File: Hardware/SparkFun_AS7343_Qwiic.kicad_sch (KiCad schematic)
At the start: 38 parts, among them J1 Qwiic_RA, J2 Qwiic_RA, J3 Conn_01x06, Q1 BSS138, Q2 BSS138, U1 RT9080-1.8V, U2 AS7343

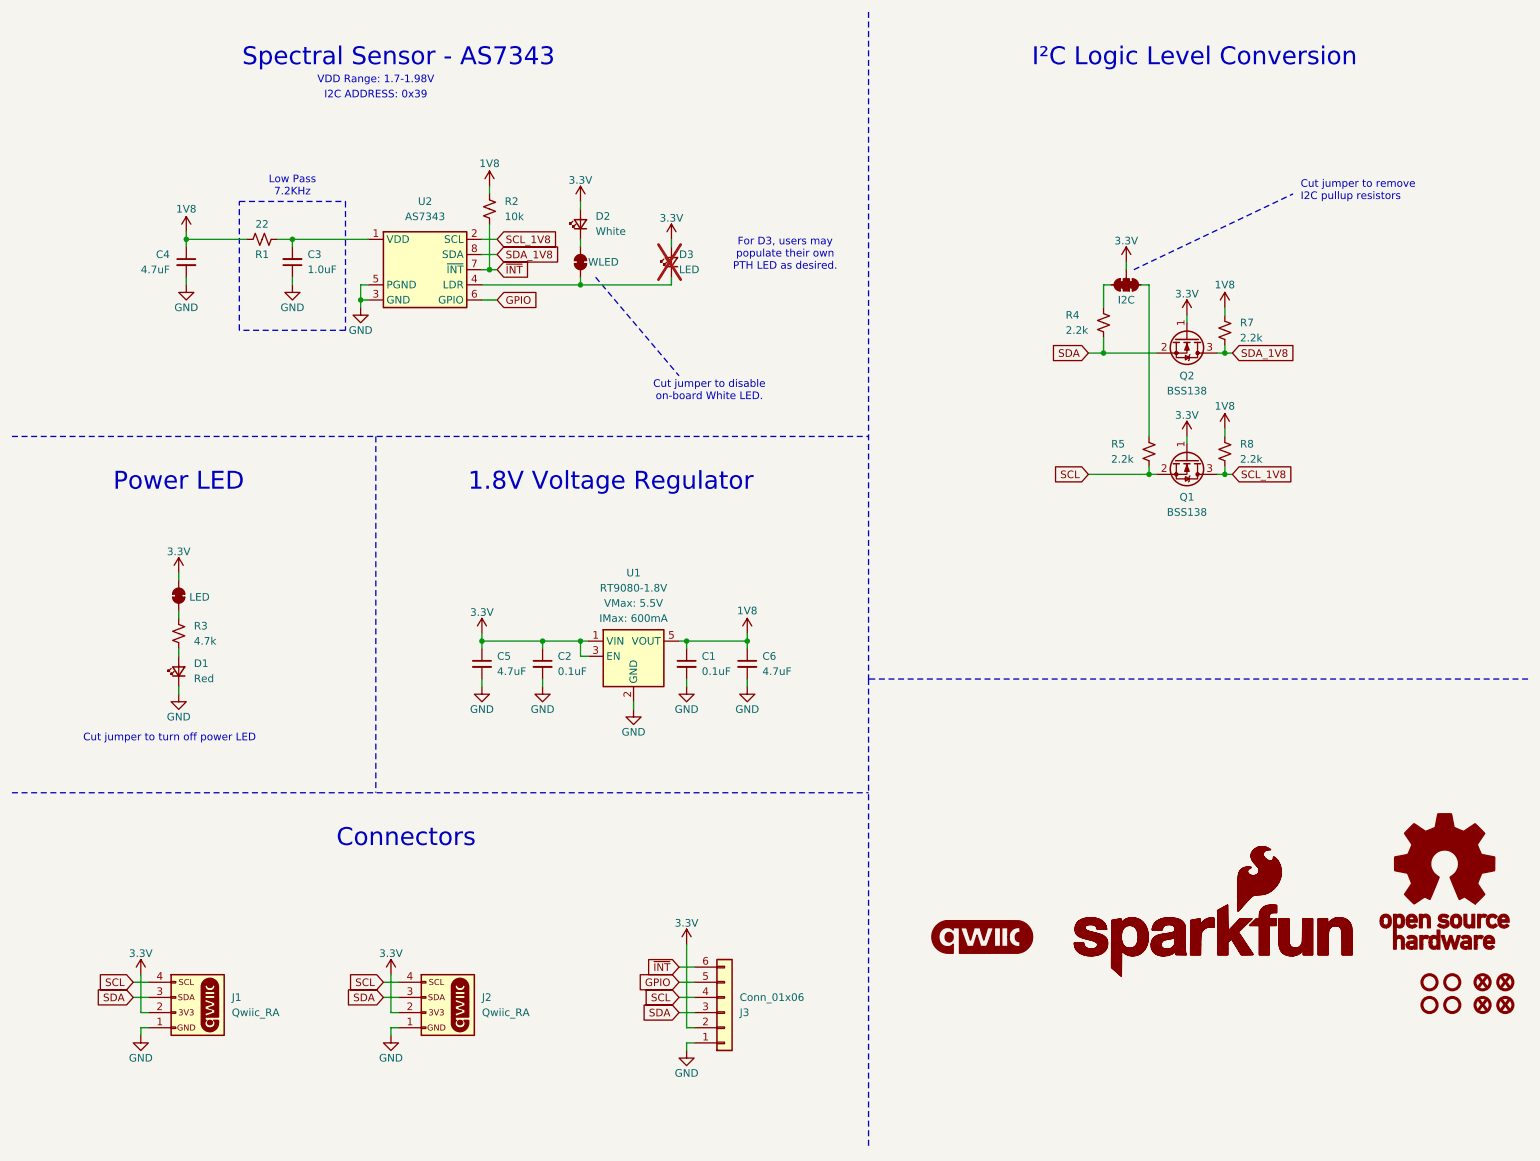
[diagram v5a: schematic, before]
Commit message: more review notes
-changed 1V8 to 1.8V to match style of 3.3V
-corrected schematic note for low pass filter. Is kHz, was KHz
-removed one of the QWIIC logos
-Moved OSHW to bottom silk
-aligned PWR LED silk label exactly with Y val of LED.
-changed sch note about i2c address to be "7-bit unshifted I2C address: 0x39"
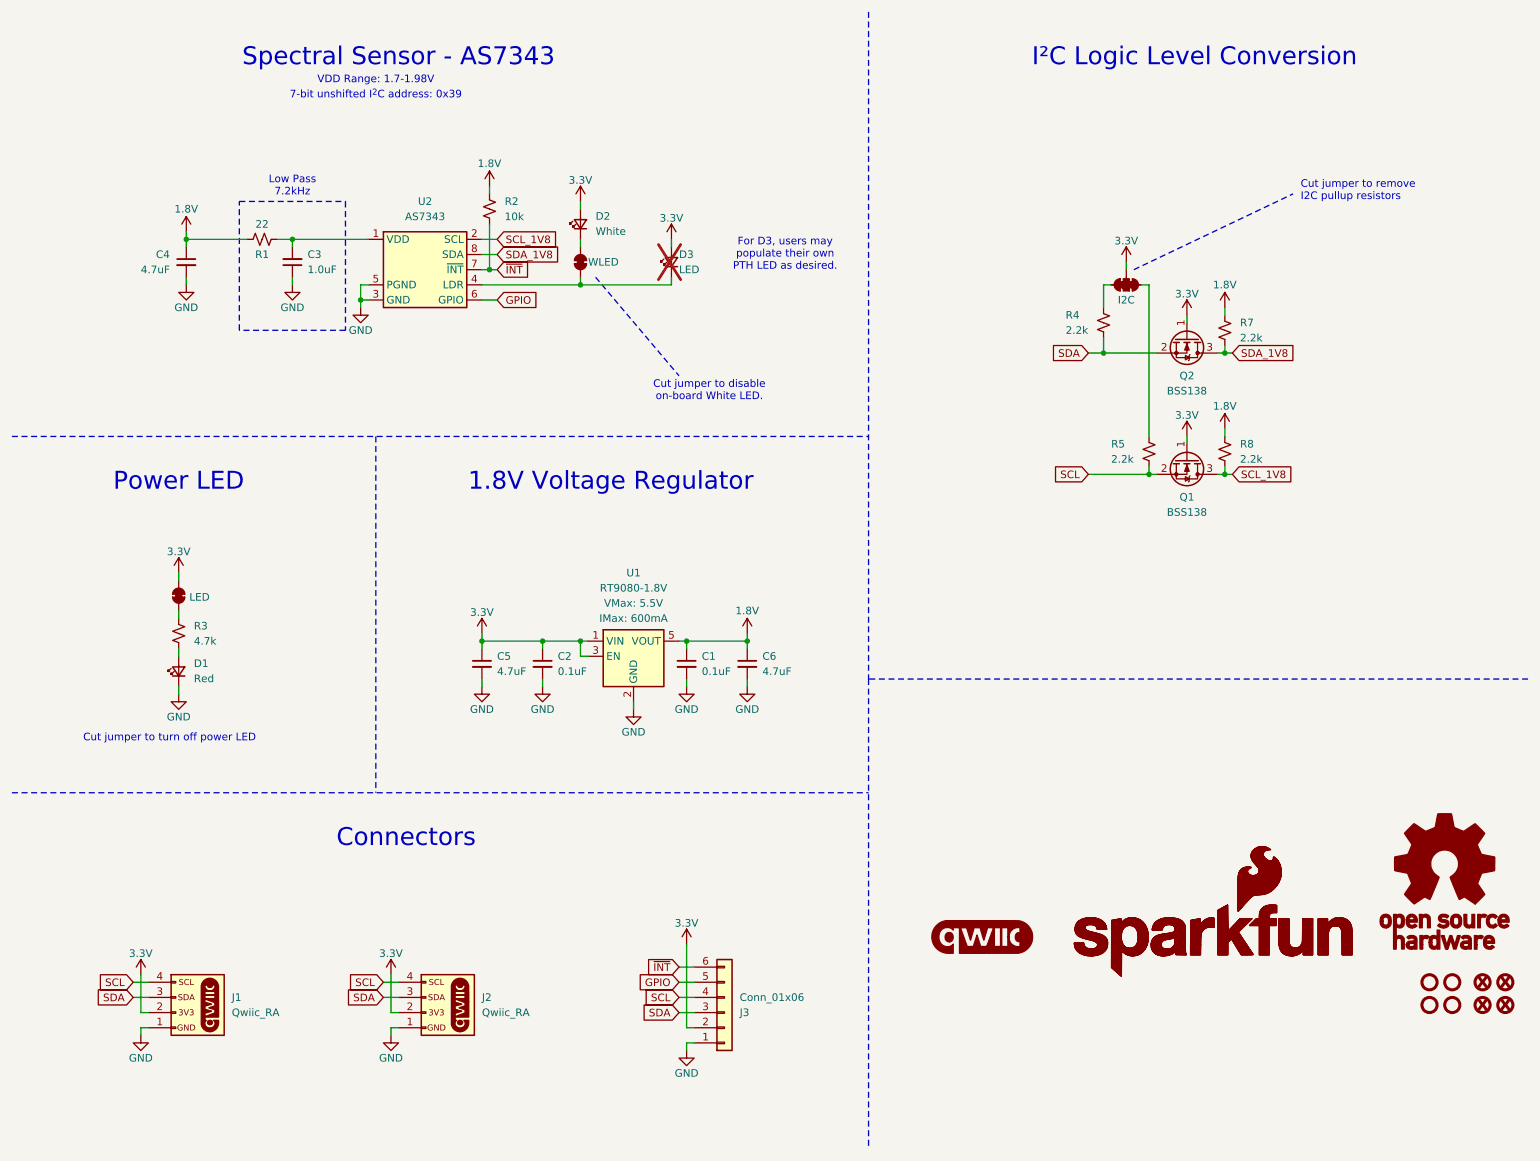
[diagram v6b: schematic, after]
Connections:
- net 1V8 renamed 1.8V
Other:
- note added: "7-bit unshifted I^{2}C address: 0x39"
- note added: "Low Pass 7.2kHz"
- note removed: "I2C ADDRESS: 0x39"
- note removed: "Low Pass 7.2KHz"
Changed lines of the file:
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@@
 		(comment 2 "Designed by: P. Lewis")
 	)
-	(text "Low Pass\n7.2KHz"
+	(text "Low Pass\n7.2kHz"
 		(exclude_from_sim no)
 		(at 59.69 41.91 0)
@@
 		)
 	)
-	(text "I2C ADDRESS: 0x39"
+	(text "7-bit unshifted I^{2}C address: 0x39"
 		(exclude_from_sim no)
 		(at 73.66 26.67 0)
@@
 			)
 		)
-		(property "Value" "1V8"
+		(property "Value" "1.8V"
 			(at 135.89 113.03 0)
 			(do_not_autoplace yes)
@@
 			)
 		)
-		(property "Value" "1V8"
+		(property "Value" "1.8V"
 			(at 215.9 78.74 0)
 			(do_not_autoplace yes)
@@
 			)
 		)
-		(property "Value" "1V8"
+		(property "Value" "1.8V"
 			(at 215.9 58.42 0)
 			(do_not_autoplace yes)
@@
 			)
 		)
-		(property "Value" "1V8"
+		(property "Value" "1.8V"
 			(at 41.91 45.72 0)
 			(do_not_autoplace yes)
@@
 			)
 		)
-		(property "Value" "1V8"
+		(property "Value" "1.8V"
 			(at 92.71 38.1 0)
 			(do_not_autoplace yes)

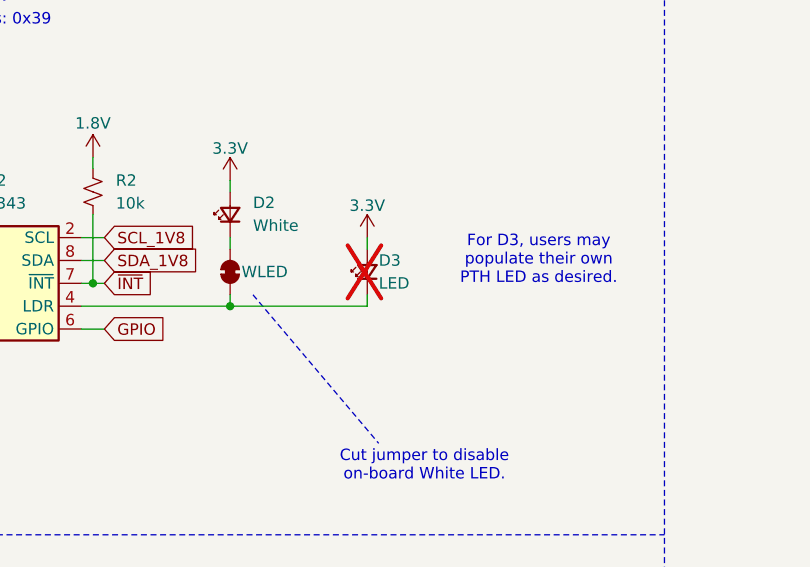
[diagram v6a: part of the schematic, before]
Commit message: added USER LED label to bottom silk
-changed value ot D3 to "USER"
-added silk label to bottom for USER LED
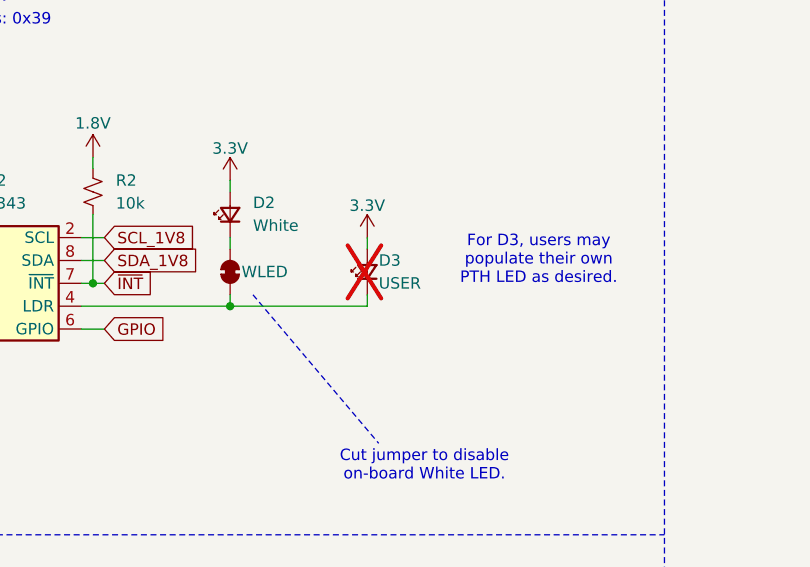
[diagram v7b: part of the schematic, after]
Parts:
- D3: value LED -> USER
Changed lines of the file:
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@@
 			)
 		)
-		(property "Value" "LED"
+		(property "Value" "USER"
 			(at 124.46 55.88 90)
 			(effects

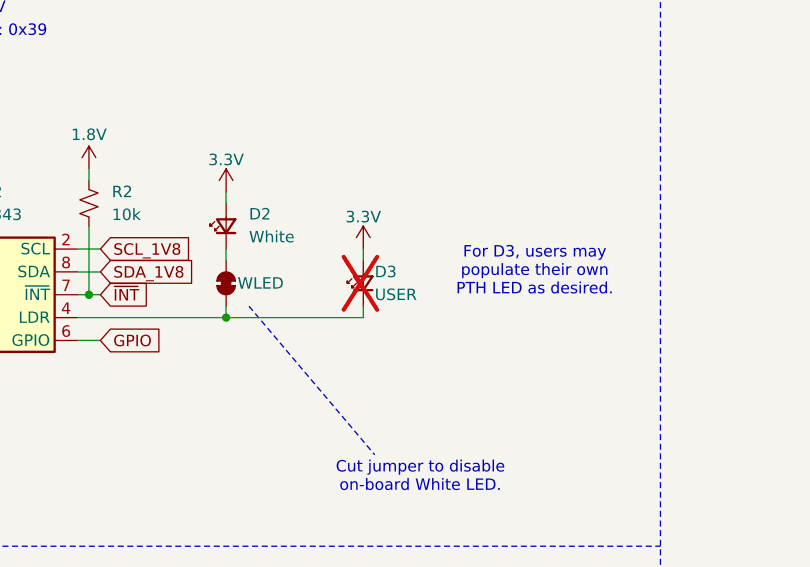
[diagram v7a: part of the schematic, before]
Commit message: library work
-updated PTH USER LED (DNP) to have fab outline and 3d model link for reference only
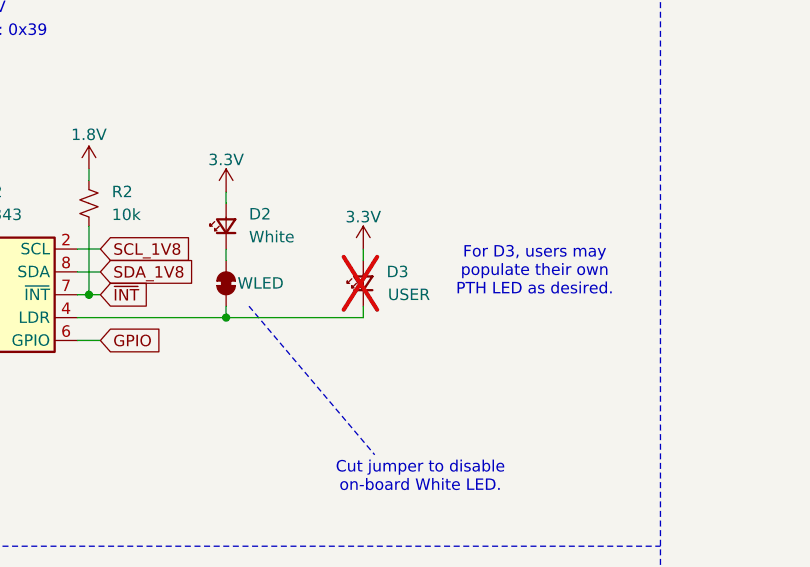
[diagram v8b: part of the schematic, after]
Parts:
- D3: footprint SparkFun-Connector:1x02 -> SparkFun-LED:LED_5MM; symbol SparkFun-LED:LED_PTH -> SparkFun-LED:LED_Red_5mm_PTH; PROD_ID (none) -> DIO-09529; now in the parts list
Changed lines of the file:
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@@
 	)
 	(symbol
-		(lib_id "SparkFun-LED:LED_PTH")
+		(lib_id "SparkFun-LED:LED_Red_5mm_PTH")
 		(at 123.19 54.61 90)
 		(unit 1)
 		(exclude_from_sim no)
-		(in_bom no)
+		(in_bom yes)
 		(on_board yes)
 		(dnp yes)
 		(property "Reference" "D3"
-			(at 124.46 53.34 90)
+			(at 127 53.34 90)
 			(effects
 				(font
 					(size 1.27 1.27)
 				)
-				(justify right)
 			)
 		)
 		(property "Value" "USER"
-			(at 124.46 55.88 90)
+			(at 128.27 55.88 90)
 			(effects
 				(font
 					(size 1.27 1.27)
 				)
-				(justify right)
 			)
 		)
-		(property "Footprint" "SparkFun-Connector:1x02"
+		(property "Footprint" "SparkFun-LED:LED_5MM"
 			(at 128.27 54.61 0)
 			(effects
@@
 			)
 		)
-		(property "Datasheet" "~"
+		(property "Datasheet" "https://cdn.sparkfun.com/assets/e/c/e/c/5/COM-09590-YSL-R531R3D-D2.pdf"
+			(at 133.35 54.61 0)
+			(effects
+				(font
+					(size 1.27 1.27)
+				)
+				(hide yes)
+			)
+		)
+		(property "Description" "Light emitting diode PTH 5mm diameter"
+			(at 135.89 54.61 0)
+			(effects
+				(font
+					(size 1.27 1.27)
+				)
+				(hide yes)
+			)
+		)
+		(property "PROD_ID" "DIO-09529"
 			(at 130.81 54.61 0)
 			(effects
@@
 			)
 		)
-		(property "Description" "Light emitting diode PTH 0.1 inch headers"
-			(at 135.89 54.61 0)
-			(effects
-				(font
-					(size 1.27 1.27)
-				)
-				(hide yes)
-			)
+		(pin "1"
 		)
 		(pin "2"
 		)
-		(pin "1"
-		)
 		(instances
